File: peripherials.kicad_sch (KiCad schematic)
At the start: 9 parts, among them J11 Hermaphroditic_Samtec_LSHM_2x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, J12 PinHeader_1x5_P2.54mm_Drill1.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, J13 PinHeader_1x3_P2.54mm_Drill1.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, U15 PN7160AHN

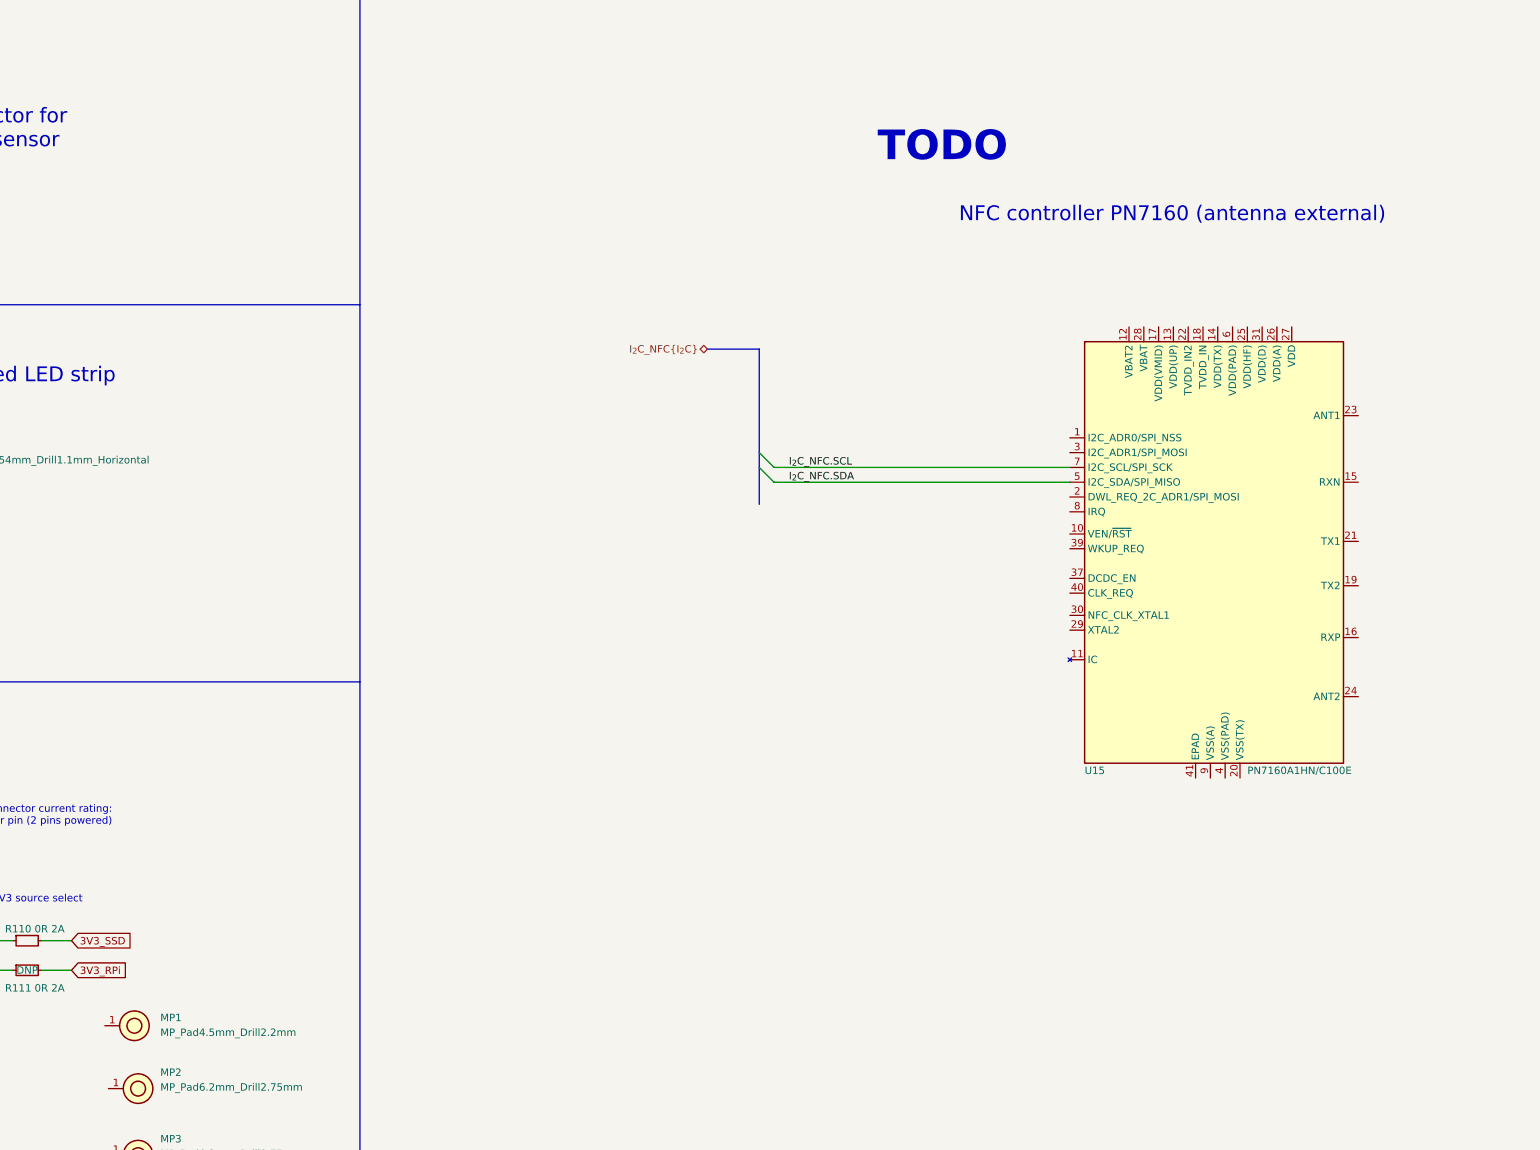
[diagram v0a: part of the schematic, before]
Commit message: [#54172] Peripherals: add passives to PN7160A, update PN7160A symbol
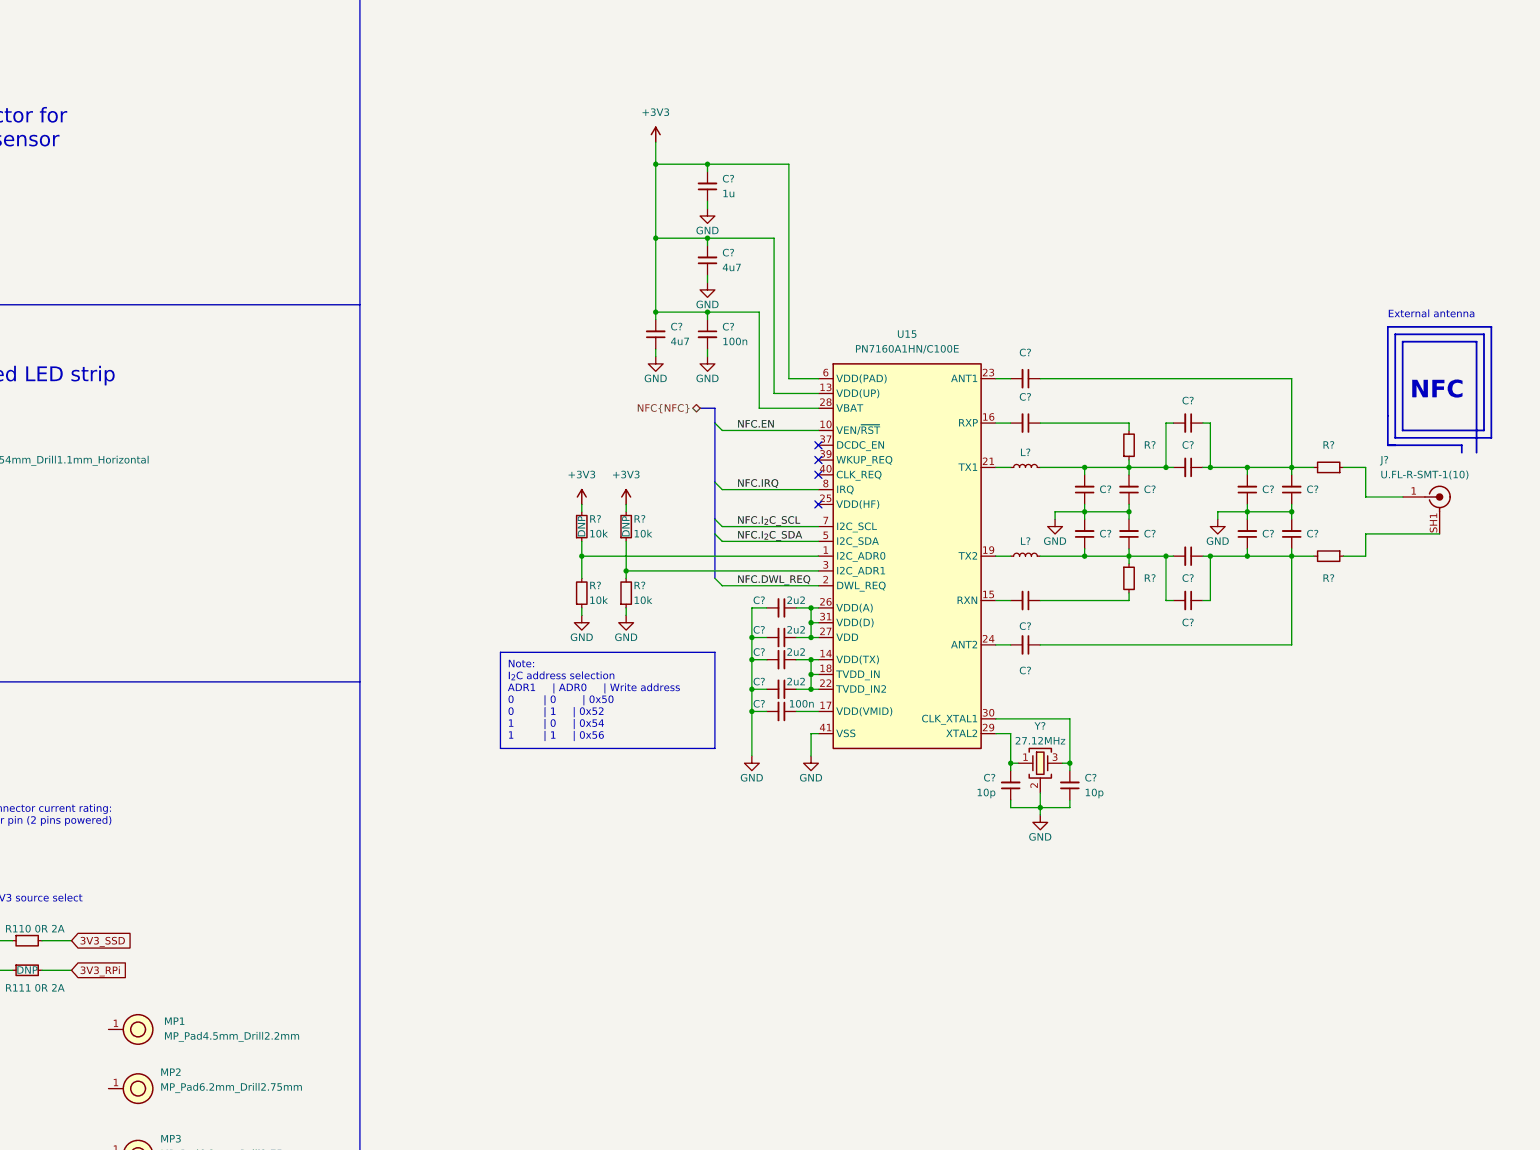
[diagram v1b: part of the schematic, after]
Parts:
- added C? (x4): C_2u2_0402, antmicro-footprints:C_0402_1005Metric, symbol antmicroCapacitors0402:C_2u2_0402
- added C? (x16): C_template_name_0402, antmicro-footprints:C_0402_1005Metric, symbol antmicroCapacitors0402:C_template_name_0402
- added C?: C_1u_0402, antmicro-footprints:C_0402_1005Metric, symbol antmicroCapacitors0402:C_1u_0402
- added C? (x2): C_4u7_0402, antmicro-footprints:C_0402_1005Metric, symbol antmicroCapacitors0402:C_4u7_0402
- added C? (x2): C_10p_0402, antmicro-footprints:C_0402_1005Metric, symbol antmicroCapacitors0402:C_10p_0402
- added C? (x2): C_100n_0402, antmicro-footprints:C_0402_1005Metric, symbol antmicroCapacitors0402:C_100n_0402
- added J?: U_FL-R-SMT-1, antmicro-footprints:Coax_Conn_U.FL, symbol antmicroCoaxialConnectorsRF:U_FL-R-SMT-1
- added L? (x2): L_template_name, antmicro-footprints:, symbol antmicroFixedInductors:L_template_name
- added R? (x4): R_template_name_0402, antmicro-footprints:R_0402_1005Metric, symbol antmicroResistors0402:R_template_name_0402
- added R? (x4): R_10k_0402, antmicro-footprints:R_0402_1005Metric, symbol antmicroResistors0402:R_10k_0402
- added Y?: Resonator_27.12MHz_XRCGB, antmicro-footprints:Oscillator_SMD_ECS_2016MV_2x1.6x0.85mm, symbol antmicroResonators:Resonator_27.12MHz_XRCGB
- U15: Manufacturer NXP Semiconductors -> NXP
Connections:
- net +3V3: now also U15.12 (VBAT2), U15.13 (VDD(UP)), U15.28 (VBAT), U15.6 (VDD(PAD)), C?.1, C?.2, C?.2, C?.2, R?.2, R?.2
- net GND: now also U15.20 (VSS(TX)), U15.4 (VSS(PAD)), U15.41 (VSS), U15.9 (VSS(A)), C?.1, C?.1, C?.1, C?.1, C?.1, C?.1, C?.1, C?.1, C?.1, C?.2, C?.2, C?.2, C?.2, C?.2, C?.2, C?.2, C?.2, C?.2, C?.2, R?.1, R?.1, Y?.2 (SH), Y?.4 (SH)
- net at U15.1 (I2C_ADR0): now also R?.1, R?.2
- net NFC.EN: now reaches U15.10 (VEN/~{RST})
- net at U15.14 (VDD(TX)): now also U15.18 (TVDD_IN), U15.22 (TVDD_IN2), C?.1, C?.1
- net at U15.15 (RXN): now also C?.2
- net at U15.16 (RXP): now also C?.2
- net at U15.17 (VDD(VMID)): now also C?.1
- net at U15.19 (TX2): now also L?.1
- net NFC.DWL_REQ: now reaches U15.2 (DWL_REQ)
- net at U15.21 (TX1): now also L?.1
- net at U15.23 (ANT1): now also C?.2
- net at U15.24 (ANT2): now also C?.2
- net at U15.26 (VDD(A)): now also U15.27 (VDD), U15.31 (VDD(D)), C?.1, C?.1
- net at U15.29 (XTAL2): now also C?.2, Y?.1
- net at U15.3 (I2C_ADR1): now also R?.1, R?.2
- net at U15.30 (CLK_XTAL1): now also C?.2, Y?.3
- net NFC.IRQ: now reaches U15.8 (IRQ)
- net I_{2}C_NFC.SCL renamed NFC.I_{2}C_SCL
- net I_{2}C_NFC.SDA renamed NFC.I_{2}C_SDA
- new net: J?.SH1, J?.SH2, R?.1
- new net: C?.1, C?.1, C?.1, C?.1, C?.1, R?.2
- new net: C?.1, C?.1, C?.1, C?.2, C?.2, R?.2
- new net: C?.2, C?.2, C?.2, C?.2, L?.2, R?.1
- new net: C?.1, C?.1, C?.2, C?.2, L?.2, R?.1
- new net: C?.1, R?.2 (x2)
- new net: J?.1, R?.1
- no-connect marks 4 -> 8
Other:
- note added: "External antenna"
- note added: "NFC"
- note added: "Note: I_{2}C address selection ADR1 | ADR0 | Write address 0 | 0 | 0x50 0 | 1 | 0x52 1 | 0 | 0x54 1 | 1 | 0x56"
- note removed: "NFC controller PN7160 (antenna external)"
- moved on the sheet: MP1

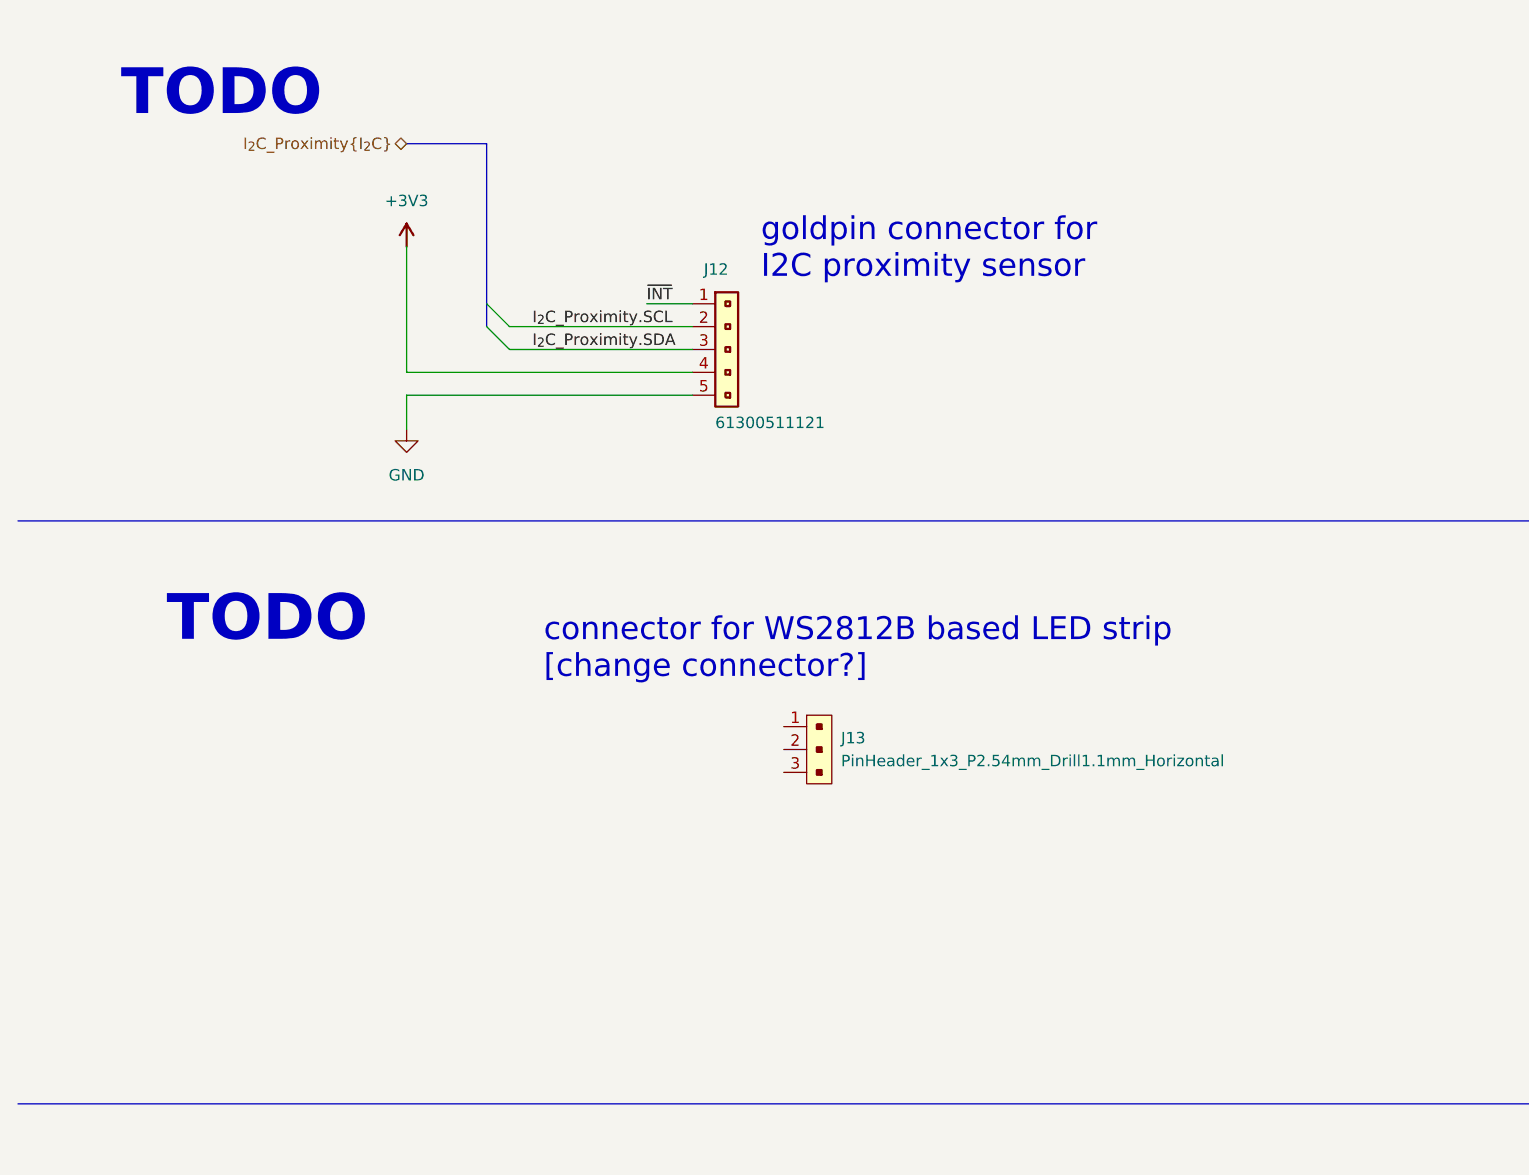
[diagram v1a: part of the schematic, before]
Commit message: [#54447] Add Sensor & LED connectors
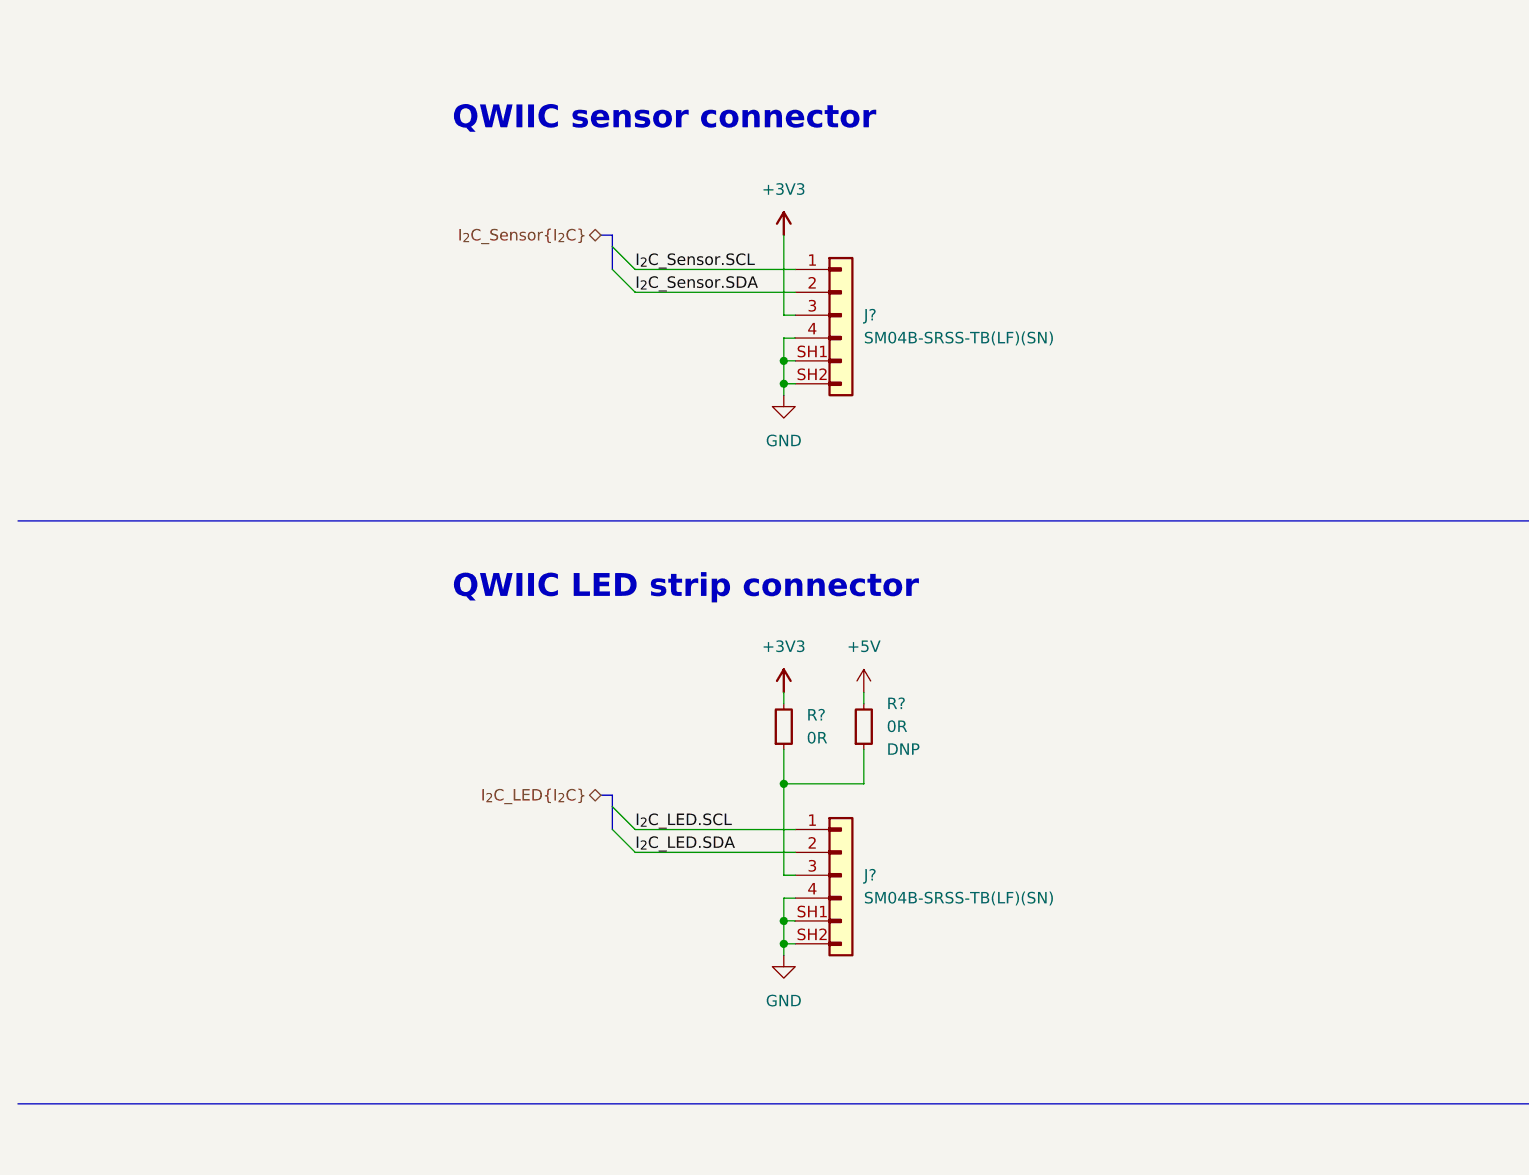
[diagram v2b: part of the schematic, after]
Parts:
- removed J12: PinHeader_1x5_P2.54mm_Drill1.1mm, antmicro-footprints:PinHeader_1x5_P2.54mm_Drill1.1mm, symbol antmicroGenericPinHeaders:PinHeader_1x5_P2.54mm_Drill1.1mm
- removed J13: PinHeader_1x3_P2.54mm_Drill1.1mm_Horizontal, antmicro-footprints:PinHeader_1x3_P2.54mm_Horizontal, symbol antmicroGenericPinHeaders:PinHeader_1x3_P2.54mm_Drill1.1mm_Horizontal
- added J? (x2): JST_SH_1x4_SM04B-SRSS-TB-LF-SN, antmicro-footprints:Conn_JST_SH_1x4_SM04B-SRSS-TB-LF-SN, symbol antmicroWire2BoardConnectors:JST_SH_1x4_SM04B-SRSS-TB-LF-SN
- added R? (x2): R_0R_0402, antmicro-footprints:R_0402_1005Metric, symbol antmicroResistors0402:R_0R_0402
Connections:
- net +3V3: now also J?.3, R?.2
- net GND: now also J?.4, J?.4, J?.SH1, J?.SH1, J?.SH2, J?.SH2
- new net: J?.3, R?.1, R?.1
- new net +5V: R?.2
- new net I_{2}C_LED.SCL: J?.1
- new net I_{2}C_LED.SDA: J?.2
- new net I_{2}C_Sensor.SCL: J?.1
- new net I_{2}C_Sensor.SDA: J?.2
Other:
- note added: "QWIIC LED strip connector"
- note added: "QWIIC sensor connector"
- note removed: "connector for WS2812B based LED strip [change connector?]"
- note removed: "goldpin connector for I2C proximity sensor"

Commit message: [#54447] Add GPIO connector
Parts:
- removed J11: Hermaphroditic_Samtec_LSHM_2x30_LSHM-130-01-L-RH-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, antmicro-footprints:Conn_Hermaphroditic_Samtec_LSHM_2x30_LSHM-130-01-XXX-RH-A-S-K-XX, symbol antmicroB2BConnectors:Hermaphroditic_Samtec_LSHM_2x30_LSHM-130-01-L-RH-A-S-K-TR
- removed MP1: MP_Pad4.5mm_Drill2.2mm, antmicro-footprints:MP_Pad4.5mm_Drill2.2mm, symbol antmicroMechanicalParts:MP_Pad4.5mm_Drill2.2mm
- removed MP2, MP3: MP_Pad6.2mm_Drill2.75mm, antmicro-footprints:MP_Pad6.2mm_Drill2.75mm, symbol antmicroMechanicalParts:MP_Pad6.2mm_Drill2.75mm
- removed R110, R111: R_0R_1206, antmicro-footprints:R_1206_3216Metric, symbol antmicroResistorsmisc:R_0R_1206
- added D? (x8): PUSB3F96X_PASS, antmicro-footprints:Nexperia_DFN-10_2.5x1mm_P0.5mm, symbol antmicroTVSDiodes:PUSB3F96X_PASS
- added J?: Socket_Samtec_ERF5_2x20_ERF5-020-05.0-L-DV-K-TR, antmicro-footprints:Conn_Socket_Samtec_ERF5_2x20_ERF5-020-05.0-L-DV-K-TR, symbol antmicroB2BConnectors:Socket_Samtec_ERF5_2x20_ERF5-020-05.0-L-DV-K-TR
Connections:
- net +3V3: now also D?.1 (CH1), D?.10 (CH1), J?.1, J?.17
- net +5V: now also D?.1 (CH1), D?.10 (CH1), J?.2, J?.4
- net GND: now also D?.3 (GND), D?.3 (GND), D?.3 (GND), D?.3 (GND), D?.3 (GND), D?.3 (GND), D?.3 (GND), D?.3 (GND), D?.8 (GND), D?.8 (GND), D?.8 (GND), D?.8 (GND), D?.8 (GND), D?.8 (GND), D?.8 (GND), D?.8 (GND), J?.20, J?.25, J?.34, J?.39, J?.6, J?.9
- new net GPIO.0/SDA1: D?.4 (CH3), D?.7 (CH3), J?.27
- new net GPIO.1/SCL1: D?.4 (CH3), D?.7 (CH3), J?.28
- new net GPIO.10: D?.5 (CH4), D?.6 (CH4), J?.19
- new net GPIO.11: D?.2 (CH2), D?.9 (CH2), J?.23
- new net GPIO.12/RXD5: D?.1 (CH1), D?.10 (CH1), J?.32
- new net GPIO.13/TXD5: D?.2 (CH2), D?.9 (CH2), J?.33
- new net GPIO.14/RXD0: D?.2 (CH2), D?.9 (CH2), J?.8
- new net GPIO.15/TXD0: D?.4 (CH3), D?.7 (CH3), J?.10
- new net GPIO.16: D?.2 (CH2), D?.9 (CH2), J?.36
- new net GPIO.17: D?.1 (CH1), D?.10 (CH1), J?.11
- new net GPIO.18: D?.5 (CH4), D?.6 (CH4), J?.12
- new net GPIO.19: D?.4 (CH3), D?.7 (CH3), J?.35
- new net GPIO.2: D?.2 (CH2), D?.9 (CH2), J?.3
- new net GPIO.20: D?.4 (CH3), D?.7 (CH3), J?.38
- new net GPIO.21: D?.5 (CH4), D?.6 (CH4), J?.40
- new net GPIO.22: D?.4 (CH3), D?.7 (CH3), J?.15
- new net GPIO.23: D?.2 (CH2), D?.9 (CH2), J?.16
- new net GPIO.24: D?.4 (CH3), D?.7 (CH3), J?.18
- new net GPIO.25: D?.5 (CH4), D?.6 (CH4), J?.22
- new net GPIO.26: D?.5 (CH4), D?.6 (CH4), J?.37
- new net GPIO.27: D?.2 (CH2), D?.9 (CH2), J?.13
- new net GPIO.3: D?.4 (CH3), D?.7 (CH3), J?.5
- new net GPIO.4/TXD3: D?.5 (CH4), D?.6 (CH4), J?.7
- new net GPIO.5/RXD3: D?.5 (CH4), D?.6 (CH4), J?.29
- new net GPIO.6: D?.1 (CH1), D?.10 (CH1), J?.31
- new net GPIO.7: D?.2 (CH2), D?.9 (CH2), J?.26
- new net GPIO.8/TXD4: D?.1 (CH1), D?.10 (CH1), J?.24
- new net GPIO.9/RXD4: D?.1 (CH1), D?.10 (CH1), J?.21
- new net GPIO.AIN0: D?.5 (CH4), D?.6 (CH4), J?.30
- new net GPIO.AIN1: D?.1 (CH1), D?.10 (CH1), J?.14
- no-connect marks 8 -> 4
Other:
- note added: "GPIO connector"
- note added: "GPIO protection"
- note added: "Note: Follows RPi connector pinout, except pins 14 & 30 (analog input)"
- note removed: "3V3 source select"
- note removed: "GPIO"
- note removed: "LSHM connector current rating: 2A per pin (2 pins powered)"
- note removed: "TODO"
- moved on the sheet: C?, J?, L?, R?, U15, Y?
